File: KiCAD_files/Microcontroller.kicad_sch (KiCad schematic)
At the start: 131 parts, among them J1 Conn_01x02, J2 RJ45_LED_Shielded, J3 RJ45_LED_Shielded, J4 Conn_01x06_Male, J5 Conn_01x06_Male, J6 Conn_01x02, J7 Power, J8 Conn_02x07_Odd_Even, J9 Conn_01x03, SW1 SW_Push, U1 STM32G474RE, U10 MCP1799T-5002H/TT, U2 AT25xxx, U3 TCAN334GDR, U4 AP1117-33, U5 UCC21222DR, U6 UCC21222DR, U7 SFH617A-2X009T, U8 RFM-0505s, U9 CME0512S3C, Y1 ECS-240-10-33-AGM-TR - 24MHz

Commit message: Created a first routed STM32G4 module and ordered it in JLCPCB
Former-commit-id: 49804de64bb80eadc7f05c9bfca13c93680f06aa
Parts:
- C15, C16, C29: symbol Device:CP1_Small -> Device:C_Polarized_Small
- FB1: symbol Device:Ferrite_Bead_Small -> Device:FerriteBead_Small
- JP1, JP2, JP4: symbol Device:Jumper -> Jumper:Jumper_2_Bridged
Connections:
- net +12V: now also C16.1
- net +12VD: now also C15.1
- net +3.3VA: now also FB1.1
- net +3V3: now also FB1.2
- net +5VD: now also JP4.1 (A)
- net +5VJP: now also JP4.2 (B)
- net +BATT: now also JP2.2 (B)
- net CAN_H: now also JP1.1 (A)
- net GNDD: now also C15.2
- net GNDREF: now also C16.2, C29.2
- net VI_high: now also C29.1
- net at BT1.1 (+): now also JP2.1 (A)
- net at R1.1: now also JP1.2 (B)
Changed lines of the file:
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@@
     (stroke (width 0) (type default) (color 0 0 0 0))
   )
+  (wire (pts (xy 41.91 267.335) (xy 48.26 267.335))
+    (stroke (width 0) (type default) (color 0 0 0 0))
+  )
   (wire (pts (xy 62.23 148.59) (xy 63.5 148.59))
     (stroke (width 0) (type default) (color 0 0 0 0))
@@
     (stroke (width 0) (type default) (color 0 0 0 0))
   )
-  (wire (pts (xy 45.72 267.335) (xy 41.91 267.335))
-    (stroke (width 0) (type default) (color 0 0 0 0))
-  )
   (wire (pts (xy 264.795 266.065) (xy 282.575 266.065))
     (stroke (width 0) (type default) (color 0 0 0 0))
@@
     (stroke (width 0) (type default) (color 0 0 0 0))
   )
-  (wire (pts (xy 197.485 220.345) (xy 197.485 224.155))
+  (wire (pts (xy 197.485 220.345) (xy 197.485 226.695))
     (stroke (width 0) (type default) (color 0 0 0 0))
   )
@@
     (stroke (width 0) (type default) (color 0 0 0 0))
   )
+  (wire (pts (xy 485.14 193.675) (xy 494.03 193.675))
+    (stroke (width 0) (type default) (color 0 0 0 0))
+  )
   (wire (pts (xy 549.91 33.02) (xy 549.91 29.21))
     (stroke (width 0) (type default) (color 0 0 0 0))
@@
     (stroke (width 0) (type default) (color 0 0 0 0))
   )
-  (wire (pts (xy 197.485 239.395) (xy 197.485 240.665))
+  (wire (pts (xy 197.485 236.855) (xy 197.485 240.665))
     (stroke (width 0) (type default) (color 0 0 0 0))
   )
@@
     (stroke (width 0) (type default) (color 0 0 0 0))
   )
-  (wire (pts (xy 60.96 267.335) (xy 67.31 267.335))
-    (stroke (width 0) (type default) (color 0 0 0 0))
-  )
   (wire (pts (xy 177.165 219.075) (xy 177.165 221.615))
     (stroke (width 0) (type default) (color 0 0 0 0))
@@
     (stroke (width 0) (type default) (color 0 0 0 0))
   )
+  (wire (pts (xy 58.42 267.335) (xy 67.31 267.335))
+    (stroke (width 0) (type default) (color 0 0 0 0))
+  )
   (wire (pts (xy 249.555 337.185) (xy 274.32 337.185))
     (stroke (width 0) (type default) (color 0 0 0 0))
@@
     (stroke (width 0) (type default) (color 0 0 0 0))
   )
-  (wire (pts (xy 487.68 193.675) (xy 494.03 193.675))
-    (stroke (width 0) (type default) (color 0 0 0 0))
-  )
   (wire (pts (xy 406.4 329.565) (xy 400.685 329.565))
     (stroke (width 0) (type default) (color 0 0 0 0))
@@
     (stroke (width 0) (type default) (color 0 0 0 0))
   )
-  (wire (pts (xy 455.295 193.675) (xy 472.44 193.675))
+  (wire (pts (xy 455.295 193.675) (xy 474.98 193.675))
     (stroke (width 0) (type default) (color 0 0 0 0))
   )
@@
     (pin "1")
   )
-  (symbol (lib_id "Device:Jumper") (at 53.34 267.335 0) (unit 1)
+  (symbol (lib_id "Jumper:Jumper_2_Bridged") (at 53.34 267.335 0) (unit 1)
     (in_bom yes) (on_board yes)
-    (property "Reference" "JP2" (id 0) (at 53.34 272.415 0))
-    (property "Value" "Jumper" (id 1) (at 54.61 274.955 0))
+    (property "Reference" "JP2" (id 0) (at 60.96 270.51 0))
+    (property "Value" "Jumper" (id 1) (at 62.23 273.05 0))
     (property "Footprint" "Connector_PinHeader_2.54mm:PinHeader_1x02_P2.54mm_Vertical" (id 2) (at 53.34 267.335 0)
       (effects (font (size 1.27 1.27)) hide)
     )
-    (property "Datasheet" "https://www.samtec.com/products/tsw-102-07-t-s" (id 3) (at 53.34 267.335 0)
+    (property "Datasheet" "~" (id 3) (at 53.34 267.335 0)
       (effects (font (size 1.27 1.27)) hide)
     )
@@
       (effects (font (size 1.27 1.27)) hide)
     )
+    (pin "1")
+    (pin "2")
   )
   (symbol (lib_id "Device:R") (at 366.395 47.625 90) (unit 1)
@@
     (pin "2")
   )
-  (symbol (lib_id "Device:Jumper") (at 197.485 231.775 270) (unit 1)
+  (symbol (lib_id "Jumper:Jumper_2_Bridged") (at 197.485 231.775 270) (unit 1)
     (in_bom yes) (on_board yes)
-    (property "Reference" "JP1" (id 0) (at 200.7108 230.6066 90)
+    (property "Reference" "JP1" (id 0) (at 204.47 229.87 90)
       (effects (font (size 1.27 1.27)) (justify left))
     )
-    (property "Value" "Jumper" (id 1) (at 200.7108 232.918 90)
+    (property "Value" "Jumper" (id 1) (at 204.47 232.41 90)
       (effects (font (size 1.27 1.27)) (justify left))
     )
@@
       (effects (font (size 1.27 1.27)) hide)
     )
+    (pin "1")
+    (pin "2")
   )
   (symbol (lib_id "Device:R") (at 381 71.755 90) (unit 1)
@@
     (pin "1")
   )
-  (symbol (lib_id "Device:CP1_Small") (at 535.94 198.755 0) (unit 1)
+  (symbol (lib_id "Device:C_Polarized_Small") (at 535.94 198.755 0) (unit 1)
     (in_bom yes) (on_board yes)
     (property "Reference" "C29" (id 0) (at 538.2514 197.5866 0)
@@
       (effects (font (size 1.27 1.27)) hide)
     )
+    (pin "1")
+    (pin "2")
   )
   (symbol (lib_id "Device:C_Small") (at 64.135 339.725 0) (unit 1)
@@
     (pin "2")
   )
-  (symbol (lib_id "Device:Ferrite_Bead_Small") (at 170.815 29.845 270) (unit 1)
+  (symbol (lib_id "Device:FerriteBead_Small") (at 170.815 29.845 270) (unit 1)
     (in_bom yes) (on_board yes)
-    (property "Reference" "FB1" (id 0) (at 170.815 23.8252 90))
-    (property "Value" "100Ohm @ 100MHz" (id 1) (at 170.815 26.1366 90))
+    (property "Reference" "FB1" (id 0) (at 147.32 24.13 90))
+    (property "Value" "100Ohm @ 100MHz" (id 1) (at 154.94 26.67 90))
     (property "Footprint" "Resistor_SMD:R_0805_2012Metric" (id 2) (at 170.815 28.067 90)
       (effects (font (size 1.27 1.27)) hide)
     )
-    (property "Datasheet" "https://www.vishay.com/docs/34025/ilbb0805.pdf" (id 3) (at 170.815 29.845 0)
+    (property "Datasheet" "~" (id 3) (at 170.815 29.845 0)
       (effects (font (size 1.27 1.27)) hide)
     )
@@
       (effects (font (size 1.27 1.27)) hide)
     )
+    (pin "1")
+    (pin "2")
   )
   (symbol (lib_id "power:+5V") (at 362.585 192.405 0) (unit 1)
@@
     (pin "3")
   )
-  (symbol (lib_id "Device:Jumper") (at 480.06 193.675 0) (unit 1)
+  (symbol (lib_id "Jumper:Jumper_2_Bridged") (at 480.06 193.675 0) (unit 1)
     (in_bom yes) (on_board yes)
-    (property "Reference" "JP4" (id 0) (at 480.06 186.9694 0))
-    (property "Value" "Jumper" (id 1) (at 480.06 189.2808 0))
+    (property "Reference" "JP4" (id 0) (at 468.63 187.96 0))
+    (property "Value" "Jumper" (id 1) (at 469.9 190.5 0))
     (property "Footprint" "Connector_PinHeader_2.54mm:PinHeader_1x02_P2.54mm_Vertical" (id 2) (at 480.06 193.675 0)
       (effects (font (size 1.27 1.27)) hide)
@@
       (effects (font (size 1.27 1.27)) hide)
     )
+    (pin "1")
+    (pin "2")
   )
   (symbol (lib_id "Device:C_Small") (at 59.69 305.435 0) (unit 1)
@@
   (symbol (lib_id "Symbols:V1.1.2") (at 184.15 140.97 0) (unit 1)
     (in_bom yes) (on_board yes)
-    (property "Reference" "#REV?" (id 0) (at 184.023 137.668 0)
+    (property "Reference" "#REV6" (id 0) (at 184.023 137.668 0)
       (effects (font (size 0.635 0.635)) hide)
     )
@@
     (pin "2")
   )
-  (symbol (lib_id "Device:CP1_Small") (at 534.035 62.23 0) (unit 1)
+  (symbol (lib_id "Device:C_Polarized_Small") (at 534.035 62.23 0) (unit 1)
     (in_bom yes) (on_board yes)
     (property "Reference" "C16" (id 0) (at 536.3464 61.0616 0)
@@
       (effects (font (size 1.27 1.27)) hide)
     )
+    (pin "1")
+    (pin "2")
   )
   (symbol (lib_id "Connector_Generic:Conn_01x02") (at 558.8 33.02 0) (unit 1)
@@
     (pin "2")
   )
-  (symbol (lib_id "Device:CP1_Small") (at 534.035 34.29 0) (unit 1)
+  (symbol (lib_id "Device:C_Polarized_Small") (at 534.035 34.29 0) (unit 1)
     (in_bom yes) (on_board yes)
     (property "Reference" "C15" (id 0) (at 536.3464 33.1216 0)
@@
       (effects (font (size 1.27 1.27)) hide)
     )
+    (pin "1")
+    (pin "2")
   )
   (symbol (lib_id "Device:R") (at 58.42 148.59 90) (unit 1)
@@
     )
     (path "/00000000-0000-0000-0000-000061fcf0e3"
-      (reference "#REV?") (unit 1) (value "V1.1.2") (footprint "")
+      (reference "#REV6") (unit 1) (value "V1.1.2") (footprint "")
     )
     (path "/00000000-0000-0000-0000-00005f54e278"

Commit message: WIP: mooving to a single board implementation with 160x100 form factor.
Former-commit-id: e8c19d5fc5237412fb5a003591d44756dbc6e173
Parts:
- removed BT1: Battery_Cell, Footprints:CR2032, symbol Device:Battery_Cell
- removed C1, C10, C11, C13, C20, C21, C22, C25, C26, C30, C31, C32, C42, C5, C7, C8, C9: 100nF, Capacitor_SMD:C_0805_2012Metric, symbol Device:C_Small
- removed C12, C41: 1µF, Capacitor_SMD:C_0805_2012Metric, symbol Device:C_Small
- removed C14: 10nF, Capacitor_SMD:C_0805_2012Metric, symbol Device:C_Small
- removed C15, C16: 47uF, Capacitor_SMD:CP_Elec_6.3x7.7, symbol Device:C_Polarized_Small
- removed C17, C18, C27, C28: 33pF, Capacitor_SMD:C_0805_2012Metric, symbol Device:C_Small
- removed C19, C24, C34, C39, C40: 10uF, Capacitor_SMD:C_1210_3225Metric, symbol Device:C_Small
- removed C23, C33: 1uF, Capacitor_SMD:C_0805_2012Metric, symbol Device:C_Small
- removed C29: 10uF, Capacitor_SMD:CP_Elec_8x11.9, symbol Device:C_Polarized_Small
- removed C3, C4: 12pF, Capacitor_SMD:C_0805_2012Metric, symbol Device:C_Small
- removed C6: 4,7uF, Capacitor_SMD:C_0805_2012Metric, symbol Device:C_Small
- removed D10, D11: STTH4R02U, Diode_SMD:D_SMB, symbol Device:D_Schottky
- removed D3, D4, D5, D6, D7, D8, D9: 3.3V, Diode_SMD:D_SOD-123, symbol Device:D_Zener_Small
- removed FB1: 100Ohm @ 100MHz, Resistor_SMD:R_0805_2012Metric, symbol Device:FerriteBead_Small
- removed J1, J6: Conn_01x02, Footprints:PTSM-0,5-2-HH0-SMD, symbol Connector_Generic:Conn_01x02
- removed J7: Power, Footprints:3D_Footprint_Power, symbol Symbols:Power
- removed J8: Conn_02x07_Odd_Even, Connector_PinHeader_1.27mm:PinHeader_2x07_P1.27mm_Vertical_SMD, symbol Connector_Generic:Conn_02x07_Odd_Even
- removed J9: Conn_01x03, Connector_PinHeader_2.54mm:PinHeader_1x03_P2.54mm_Vertical, symbol Connector_Generic:Conn_01x03
- removed JP2: Jumper, Connector_PinHeader_2.54mm:PinHeader_1x02_P2.54mm_Vertical, symbol Jumper:Jumper_2_Bridged
- removed LED1: LED, LED_SMD:LED_0805_2012Metric, symbol Device:LED
- removed LED2: PWR, LED_SMD:LED_0805_2012Metric, symbol Device:LED
- removed PS5: VXO78xxx, CONV_VXO78012-500-M, symbol Symbols:VXO78xxx
- removed R14, R17, R18, R21, R9: 51, Resistor_SMD:R_0805_2012Metric, symbol Device:R
- removed R15, R19: 20k, Resistor_SMD:R_0805_2012Metric, symbol Device:R
- removed R16, R20: 2.2, Resistor_SMD:R_0805_2012Metric, symbol Device:R
- removed R2, R24, R3, R4, R5, R6, R7, R8: 100, Resistor_SMD:R_0805_2012Metric, symbol Device:R
- removed R22: 1k, Resistor_SMD:R_0805_2012Metric, symbol Device:R
- removed R23: 220, Resistor_SMD:R_0805_2012Metric, symbol Device:R
- removed R26, R28: 330, Resistor_SMD:R_0805_2012Metric, symbol Device:R
- removed SW1: SW_Push, Button_Switch_SMD:SW_Push_1P1T_NO_CK_KMR2, symbol Switch:SW_Push
- removed SWD1: Conn_01x06_Female, Connector_PinHeader_2.54mm:PinHeader_1x06_P2.54mm_Vertical, symbol Connector:Conn_01x06_Female
- removed TP1, TP12, TP13, TP14, TP15, TP2, TP3, TP4, TP5, TP6, TP7, TP8: TestPoint, TestPoint:TestPoint_THTPad_D2.0mm_Drill1.0mm, symbol Connector:TestPoint
- removed U1: STM32G474RE, Package_QFP:LQFP-64_10x10mm_P0.5mm, symbol Symbols:STM32G474RE
- removed U2: AT25xxx, Footprints:SOIC-8_3.9x4.9mm_P1.27mm, symbol Memory_EEPROM:AT25xxx
- removed U4: AP1117-33, Package_TO_SOT_SMD:SOT-223-3_TabPin2, symbol Regulator_Linear:AP1117-33
- removed U5, U6: UCC21222DR, Package_SO:SOIC-16W_7.5x10.3mm_P1.27mm, symbol Driver_FET:UCC21520DW
- removed U7: SFH617A-2X009T, Package_DIP:SMDIP-4_W7.62mm, symbol Isolator:SFH617A-2X009T
- removed U8: RFM-0505s, Converter_DCDC:Converter_DCDC_muRata_CRE1xxxxxx3C_THT, symbol Symbols:RFM-0505s
- removed U9: CME0512S3C, Converter_DCDC:Converter_DCDC_muRata_CRE1xxxxxx3C_THT, symbol Symbols:RFM-0505s
- removed Y1: ECS-240-10-33-AGM-TR - 24MHz, Crystal:Crystal_SMD_3225-4Pin_3.2x2.5mm, symbol Device:Crystal_GND24
- added C404, C405: 4.7u, Capacitor_SMD:C_1210_3225Metric, symbol Device:C_Small
- added C410: C_Polarized_Small, Capacitor_SMD:CP_Elec_10x10.5, symbol Device:C_Polarized_Small
- added JP403, JP404: Jumper, Connector_PinHeader_2.54mm:PinHeader_1x02_P2.54mm_Vertical, symbol Jumper:Jumper_2_Bridged
- added L401: L_Small, symbol Device:L_Small
- added P401: Power2, symbol Symbols:Power2
- added PS401: MEE1S0505SC, Footprints:Converter_DCDC_Murata_MEE1SxxxxSC_THT, symbol Converter_DCDC:MEE1S0505SC
- added PS402: MEE1S0512SC, Footprints:Converter_DCDC_Murata_MEE1SxxxxSC_THT, symbol Converter_DCDC:MEE1S0512SC
- added R407: 20k, Resistor_SMD:R_0805_2012Metric, symbol Device:R
- added TH402: NXFT15XH103FA2B100, Connector_PinHeader_1.27mm:PinHeader_1x02_P1.27mm_Horizontal, symbol Device:Thermistor
- added U401: OwnTech, Footprints:OwnTech_MCU, symbol Symbols:OwnTech_MCU
- JP401: renamed from JP1; footprint Jumper:SolderJumper-2_P1.3mm_Open_Pad1.0x1.5mm -> Connector_PinHeader_2.54mm:PinHeader_1x02_P2.54mm_Vertical; DNP x -> (none)
- PS403: renamed from PS4; value PQDE6W-Q110-S5-D -> Feeder; footprint CONV_VXO78012-500-M -> Footprints:Feeder; symbol Symbols:PQDE6W-Q110-S5-D -> Symbols:Feeder; MANUFACTURER CUI Inc. -> OwnTech; MAXIMUM_PACKAGE_HEIGHT 3.5 mm -> (none); Manf# PQDE6W-Q110-S5-D -> (none); PARTREV 1.0 -> (none); STANDARD Manufacturer Recommendations -> (none)
- renumbered C2 to C401, C38 to C402, C37 to C403, C35 to C406, C36 to C407, C44 to C408, C43 to C409, D1 to D401, D2 to D402, F1 to F401, F2 to F402, J4 to J401, J5 to J402, J2 to J403, J3 to J404, JP3 to JP402, JP4 to JP405, R1 to R401, R10 to R402, R11 to R403, R12 to R404, R13 to R405, R25 to R406, TH1 to TH401, TP32 to TP401, TP33 to TP402, U3 to U402, U10 to U403
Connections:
- net VI_high is gone; now on net DGND: PS403.3 (-VO)
- net +12V: now also PS402.4 (+Vout)
- net +3V3: now also JP403.2 (B), R407.2, U401.42 (+3.3V)
- net +5VD: now also C410.1, P401.27 (+5VD), PS401.2 (+Vin), PS402.2 (+Vin), U401.46 (+VIN)
- net +BATT: now also U401.45 (+VBAT)
- net DAC2: now also U401.40 (PA6)
- net N_GND: now also P401.9 (NGND_{cmd})
- net Temp: now also U401.43 (PB1)
- net +5V renamed +5VN
- net +5VN: now also P401.31 (+5VN), PS401.4 (+Vout)
- net FDCAN1_RX renamed FDCAN1_{RX}
- net FDCAN1_{RX}: now also U401.26 (PB8)
- net FDCAN1_TX renamed FDCAN1_{TX}
- net FDCAN1_{TX}: now also U401.27 (PB9)
- net GNDD renamed DGND
- net DGND: now also C410.2, JP404.1 (A), P401.28 (NGND), P401.30 (DGND), PS401.1 (-Vin), PS402.1 (-Vin), TH402.2, U401.13 (GND), U401.18 (GND), U401.22 (GND), U401.25 (GND), U401.29 (GND), U401.3 (GND), U401.34 (GND), U401.39 (GND), U401.44 (GND), U401.8 (GND); no longer J403.SH, J404.SH, PS403.6 (-VO)
- net GNDREF renamed GND
- net GND: now also C405.2, P401.33 (GND), PS402.3 (-Vout)
- net N renamed NGND
- net NGND: now also P401.28 (NGND), PS401.3 (-Vout)
- net SPI3_MISO renamed SPI3_{MISO}
- net SPI3_{MISO}: now also U401.20 (PB4)
- net SPI3_MOSI renamed SPI3_{MOSI}
- net SPI3_{MOSI}: now also U401.21 (PB5)
- net USART1_RX renamed USART1_{RX}
- net USART1_{RX}: now also U401.24 (PB7)
- net USART1_TX renamed USART1_{TX}
- net USART1_{TX}: now also U401.23 (PB6)
- net VREF1024 renamed VREF
- net VREF: now also P401.29 (VREF)
- new net: L401.2, PS403.1 (+VIN)
- new net: C404.2, C405.1
- new net +5VP: P401.33 (GND)
- new net BOOT: JP403.1 (A), U401.37 (PB0)
- new net HRTIM_CHA1: P401.1 (GH2), U401.14 (PA9)
- new net HRTIM_CHA2: P401.3 (GL2), U401.12 (PA8)
- new net HRTIM_CHC1: P401.1 (GH2), U401.2 (PB12)
- new net HRTIM_CHC2: P401.3 (GL2), U401.4 (PB13)
- new net I_{I1Low}: P401.19 (I_{I1Low}), U401.36 (PA1)
- new net I_{I2Low}: P401.21 (I_{I2Low}), U401.31 (PC1)
- new net I_{IHigh}: P401.23 (I_{IHigh}), U401.32 (PC2)
- new net PC13: JP404.2 (B), U401.28 (PC13)
- new net Temp2: R407.1, TH402.1
- new net V_{I1Low}: P401.13 (V_{I1Low}), U401.35 (PA0)
- new net V_{I2Low}: P401.15 (V_{I2Low}), U401.30 (PC0)
- new net V_{IHighfeeder}: C404.1, L401.1, P401.33 (GND)
- new net V_{IHigh}: P401.17 (V_{IHigh}), U401.33 (PC3)
- no-connect marks 10 -> 20
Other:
- note removed: "24Mhz HSE freq is choosen to match NucleoG474RE design."
- note removed: "C3 and C4 are choosen following the rule of thumb : C3 = C4 = 2*CLoad - 2*CStray Where CStray is the parasitic capacitance Guesstimated at 4pF."
- note removed: "Decoupling capacitors choosen as per datasheet 5.16 Power supply scheme fig.16"
- note removed: "EEPROM - SPI"
- note removed: "I1 is tied to PC1 which is ADC2 CH2 or COMP1 INP (in current mode)"
- note removed: "I2 is tied to PC1 which is ADC1 CH7 or COMP3 INP (in current mode)"
- note removed: "MCU protections from analog inputs"
- note removed: "Only one footprint to be populated depending if the converter is powered from a DAB module or is standalone"
- note removed: "Power input terminals for MCU and power side"
- note removed: "Real Time Clock Battery"
- note removed: "STDC14 / ARM10 connector for debugger connection Compatible with STLINKV3"
- note removed: "SWD connector"
- note removed: "Zener diodes protect from potential overvoltages while resistors prevent accidental high current flow"
- moved on the sheet: C401, C402, C403, C406, C407, C408, C409, D401, D402, F401, F402, J401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

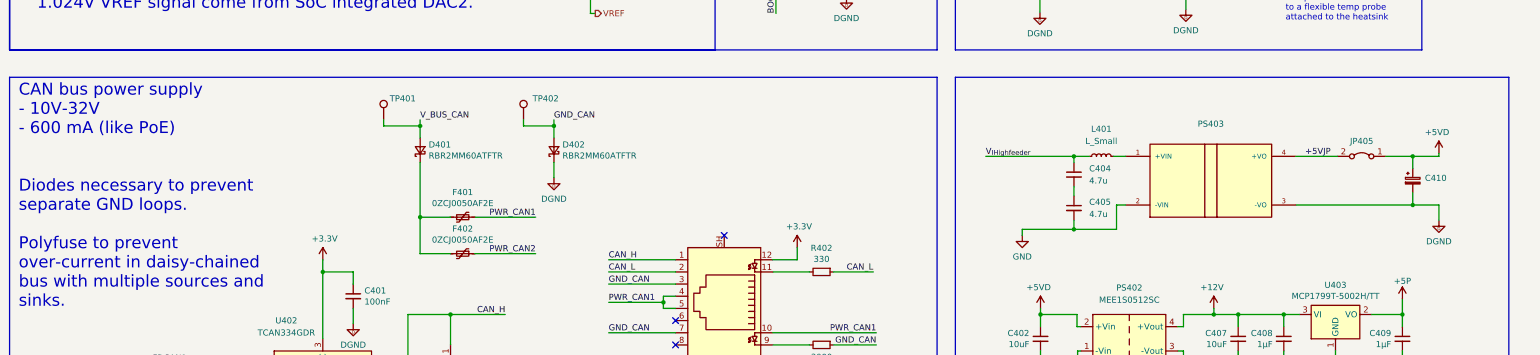
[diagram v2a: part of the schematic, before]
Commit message: WIP: integrated the feeder on the power board directly
Former-commit-id: e81265b44c994f7ae6e14a178f616f328de7a2ab
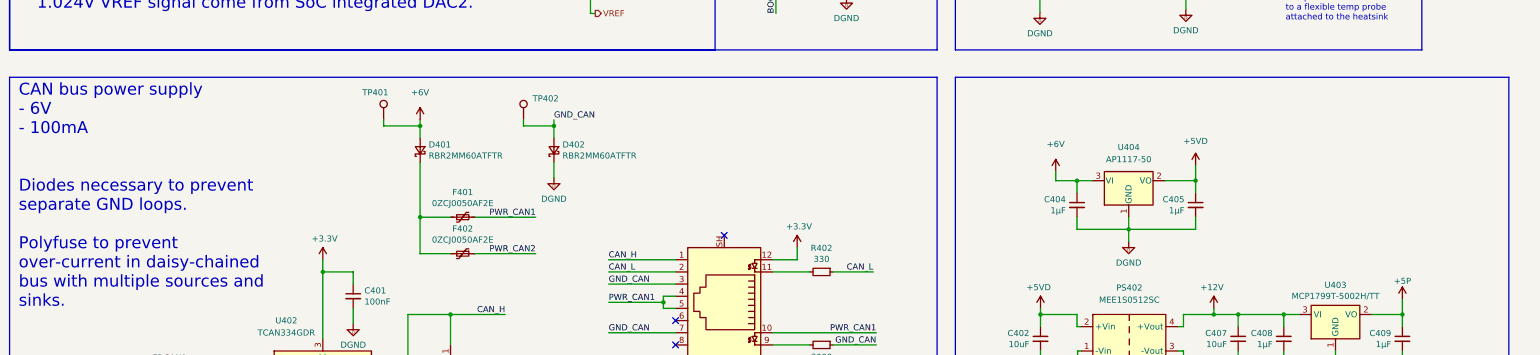
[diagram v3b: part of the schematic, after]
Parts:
- removed C410: C_Polarized_Small, Capacitor_SMD:CP_Elec_10x10.5, symbol Device:C_Polarized_Small
- removed JP405: Jumper, Connector_PinHeader_2.54mm:PinHeader_1x02_P2.54mm_Vertical, symbol Jumper:Jumper_2_Bridged
- removed L401: L_Small, symbol Device:L_Small
- removed PS403: Feeder, Footprints:Feeder, symbol Symbols:Feeder
- added U404: AP1117-50, Package_TO_SOT_SMD:SOT-223-3_TabPin2, symbol Regulator_Linear:AP1117-50
- C404, C405: value 4.7u -> 1µF; footprint Capacitor_SMD:C_1210_3225Metric -> Capacitor_SMD:C_0805_2012Metric; Manf# (none) -> CL21B105KBFNFNE
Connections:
- net +5VD: now also C405.1, U404.2 (VO)
- net DGND: now also C404.2, C405.2, U404.1 (GND)
- net GND: no longer C405.2
- net V_{IHighfeeder}: no longer C404.1
- net V_BUS_CAN renamed +6V
- net +6V: now also C404.1, U404.3 (VI)
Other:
- note added: "CAN bus power supply - 6V - 100mA Diodes necessary to prevent separate GND loops. Polyfuse to prevent over-current in daisy-chained bus with multiple sources and sinks."
- note removed: "CAN bus power supply - 10V-32V - 600 mA (like PoE) Diodes necessary to prevent separate GND loops. Polyfuse to prevent over-current in daisy-chained bus with multiple sources and sinks."

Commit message: WIP : 99 percents of the nets are now routed properly
Former-commit-id: fcbb95e3f0a6512a63faba729c3990d7109d7768
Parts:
- removed TP401, TP402: TestPoint, TestPoint:TestPoint_THTPad_D2.0mm_Drill1.0mm, symbol Connector:TestPoint
- added R408: 1R, Resistor_SMD:R_0805_2012Metric, symbol Device:R
- F401, F402: footprint Fuse:Fuse_1812_4532Metric -> Fuse:Fuse_0805_2012Metric
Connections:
- net DGND: now also R408.2; no longer C405.2
- net Earth_Protective: now reaches J403.SH
- net Earth_Protective: now also J404.SH
- new net: C405.2, R408.1
- no-connect marks 20 -> 18
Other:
- moved on the sheet: C404, C405, U404

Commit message: WIP : Routed last sensors to the MCU, tweaked the courtiyards ERC almost passing
Former-commit-id: ade1cde8d39341e78235fc8e83a4a1c667a0d829
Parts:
- removed JP404: Jumper, Connector_PinHeader_2.54mm:PinHeader_1x02_P2.54mm_Vertical, symbol Jumper:Jumper_2_Bridged
- added JP404, JP405, JP406: Jumper_2_Bridged, Jumper:SolderJumper-2_P1.3mm_Bridged_Pad1.0x1.5mm, symbol Jumper:SolderJumper_2_Bridged
- added JP407: Jumper, Connector_PinHeader_2.54mm:PinHeader_1x02_P2.54mm_Vertical, symbol Jumper:Jumper_2_Open
- C401, C404, C405, C408, C409: footprint Capacitor_SMD:C_0805_2012Metric -> Footprints:C_0805_2012Metric
- C402, C403, C406, C407: footprint Capacitor_SMD:C_1210_3225Metric -> Footprints:C_1210_3225Metric
- JP402: footprint Jumper:SolderJumper-2_P1.3mm_Open_Pad1.0x1.5mm -> Jumper:SolderJumper-2_P1.3mm_Bridged_Pad1.0x1.5mm; symbol Jumper:SolderJumper_2_Open -> Jumper:SolderJumper_2_Bridged
- JP403: symbol Jumper:Jumper_2_Bridged -> Jumper:Jumper_2_Open
- R401, R402, R403, R404, R405, R406, R407, R408: footprint Resistor_SMD:R_0805_2012Metric -> Footprints:R_0805_2012Metric
- U403: footprint Package_TO_SOT_SMD:SOT-23 -> Footprints:SOT-23_copy
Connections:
- net DGND: now also JP407.2 (B)
- net PC13: now also JP407.1 (A)
- net Temp: now also JP406.2 (B); no longer U401.43 (PB1)
- net Temp2: now also JP405.2 (B)
- net PC6: now reaches U401.7 (PC6)
- net PC6: now also JP404.2 (B)
- net BOOT renamed ADC3_IN12
- net ADC3_IN12: now also JP405.1 (A)
- net N_GND renamed N_{GND}
- net N_{GND}: now also JP404.1 (A)
- new net ADC3_IN1: JP406.1 (A), U401.43 (PB1)
- no-connect marks 18 -> 17
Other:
- moved on the sheet: JP403

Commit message: WIP : Started correcting MCU board mistakes
Former-commit-id: 0e34b6d72e10d1eac13c8cf31fc8e8f14d7f468b
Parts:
- added TP401, TP402, TP403, TP404, TP405, TP406, TP407, TP408: TestPoint, TestPoint:TestPoint_Pad_D1.0mm, symbol Connector:TestPoint
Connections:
- net ADC3_IN12: no longer JP403.1 (A)
- net DGND: now also TP405.1, TP406.1, TP407.1, TP408.1
- net HRTIM_CHA1: now also TP403.1
- net HRTIM_CHA2: now also TP404.1
- net HRTIM_CHC1: now also TP401.1
- net HRTIM_CHC2: now also TP402.1
- net FDCAN1_{RX} renamed BOOT
- net BOOT: now also JP403.1 (A)
